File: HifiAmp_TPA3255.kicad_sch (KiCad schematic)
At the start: 125 parts, among them J1 PVDD 48V IN — NEEDS_DATA, J2 RCA L SE, J3 RCA R SE, J301 SPK_L, J302 SPK_R, J4 VOLUME_REMOTE, Q301 IPP330P10NM, Q302 IXTK200N10L2, U1 LM5010ASD, U2 LM2940IMP-12/NOPB, U3 TLV1117-33IDCY, U4 OPA1612AIDR, U5 OPA1612AIDR, U6 TPA3255B, U7 TPS3802K33DCKR, U8 LM5069-2

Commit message: feat(f1.7): add the WE-PD 1050 footprint, assign correct U1/L1 footprints in the schematic
Co-Authored-By: Claude Opus 5.5 <noreply@anthropic.com>
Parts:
- L1: footprint Inductor_SMD:L_Wuerth_WE-PD2-Typ-MS -> HifiAmp_TPA3255_Local:L_Wuerth_WE-PD-1050_10x10x5mm
- U1: footprint Package_SON:WSON-10-1EP_2.5x2.5mm_P0.5mm_EP1.2x2mm -> Package_SON:WSON-10-1EP_4x4mm_P0.8mm_EP2.6x3mm
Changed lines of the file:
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@@
 			)
 		)
-		(property "Footprint" "Package_SON:WSON-10-1EP_2.5x2.5mm_P0.5mm_EP1.2x2mm"
+		(property "Footprint" "Package_SON:WSON-10-1EP_4x4mm_P0.8mm_EP2.6x3mm"
 			(at 100.33 100.33 0)
 			(hide yes)
@@
 			)
 		)
-		(property "Footprint" "Inductor_SMD:L_Wuerth_WE-PD2-Typ-MS"
+		(property "Footprint" "HifiAmp_TPA3255_Local:L_Wuerth_WE-PD-1050_10x10x5mm"
 			(at 129.54 100.33 0)
 			(hide yes)

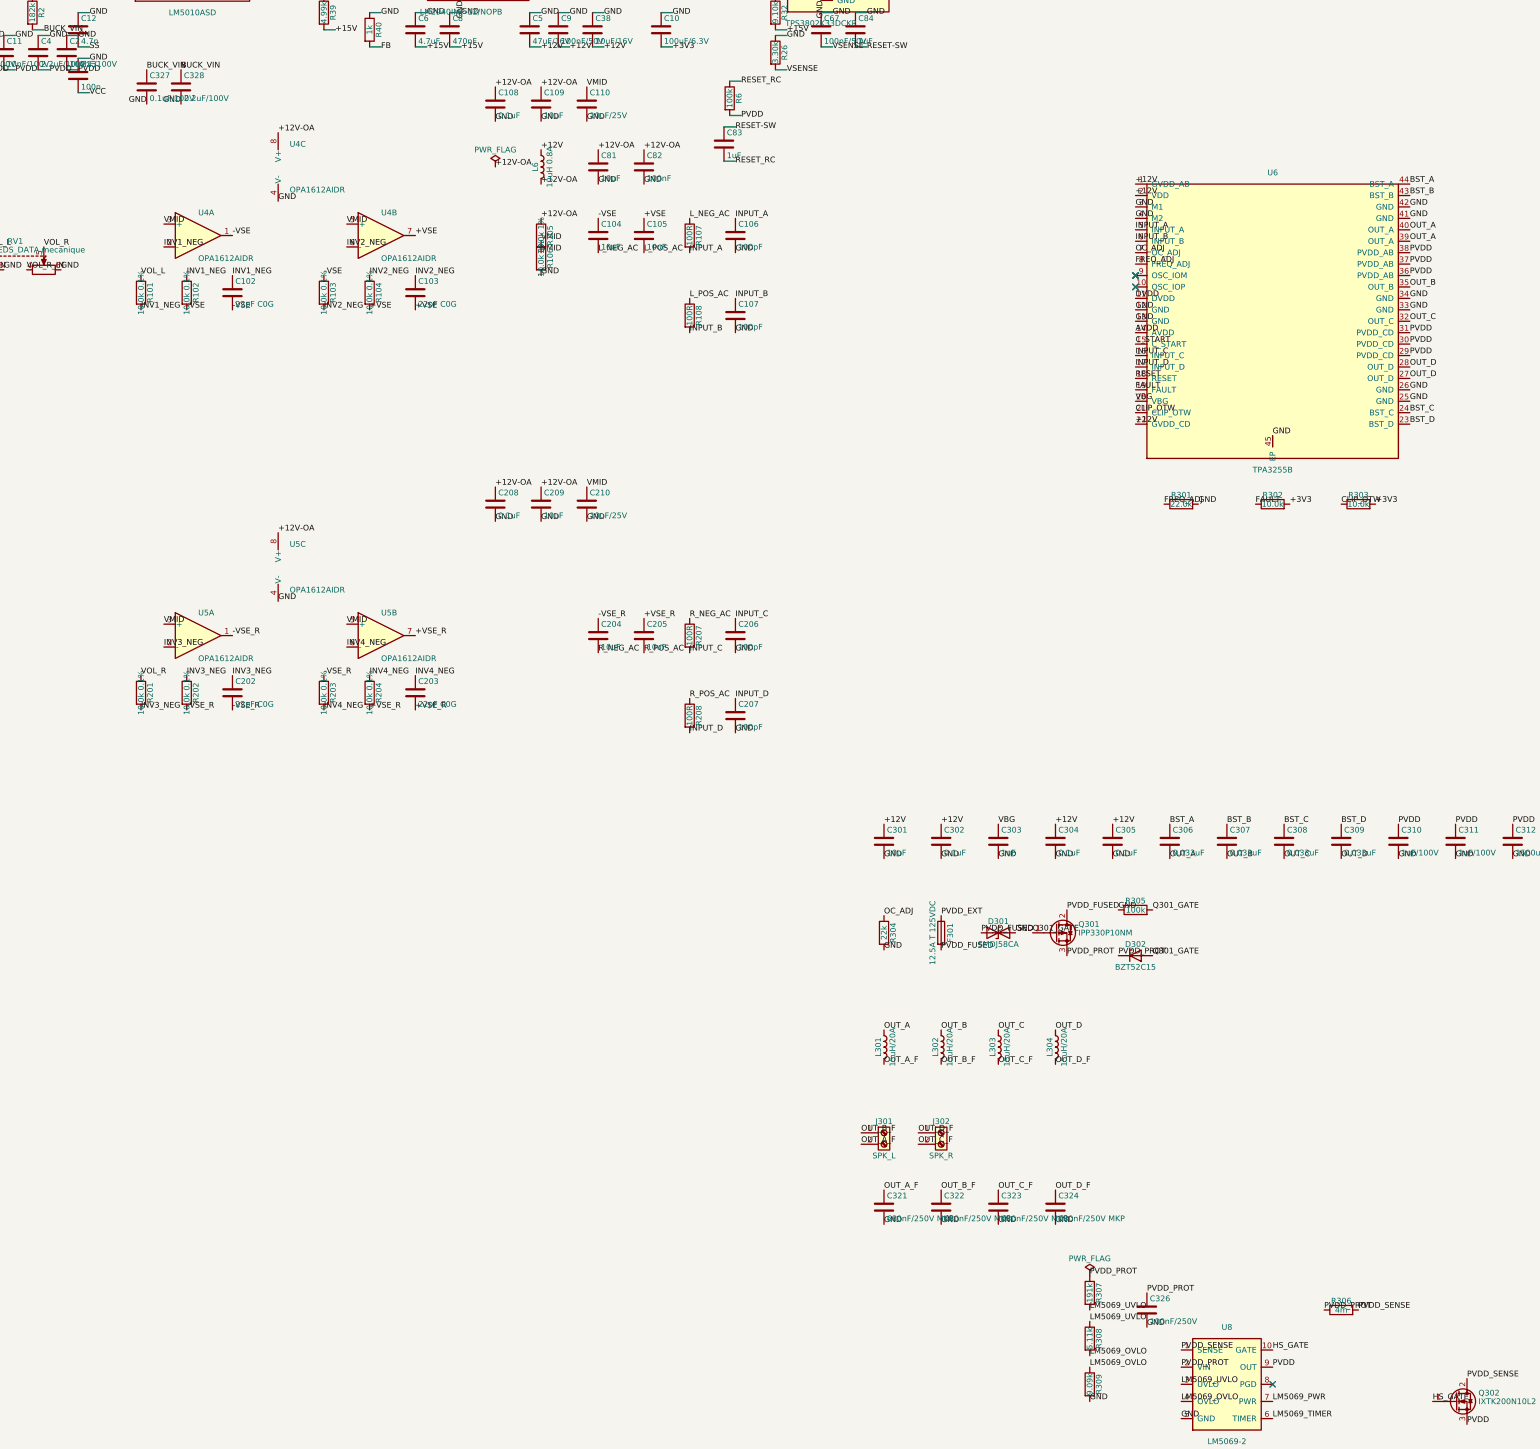
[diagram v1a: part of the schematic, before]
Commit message: feat(g1.3-b): set C13 to 1 µF, add C329 1 µF/100 V on PVDD_SENSE in the schematic
Co-Authored-By: Claude Opus 5.5 <noreply@anthropic.com>
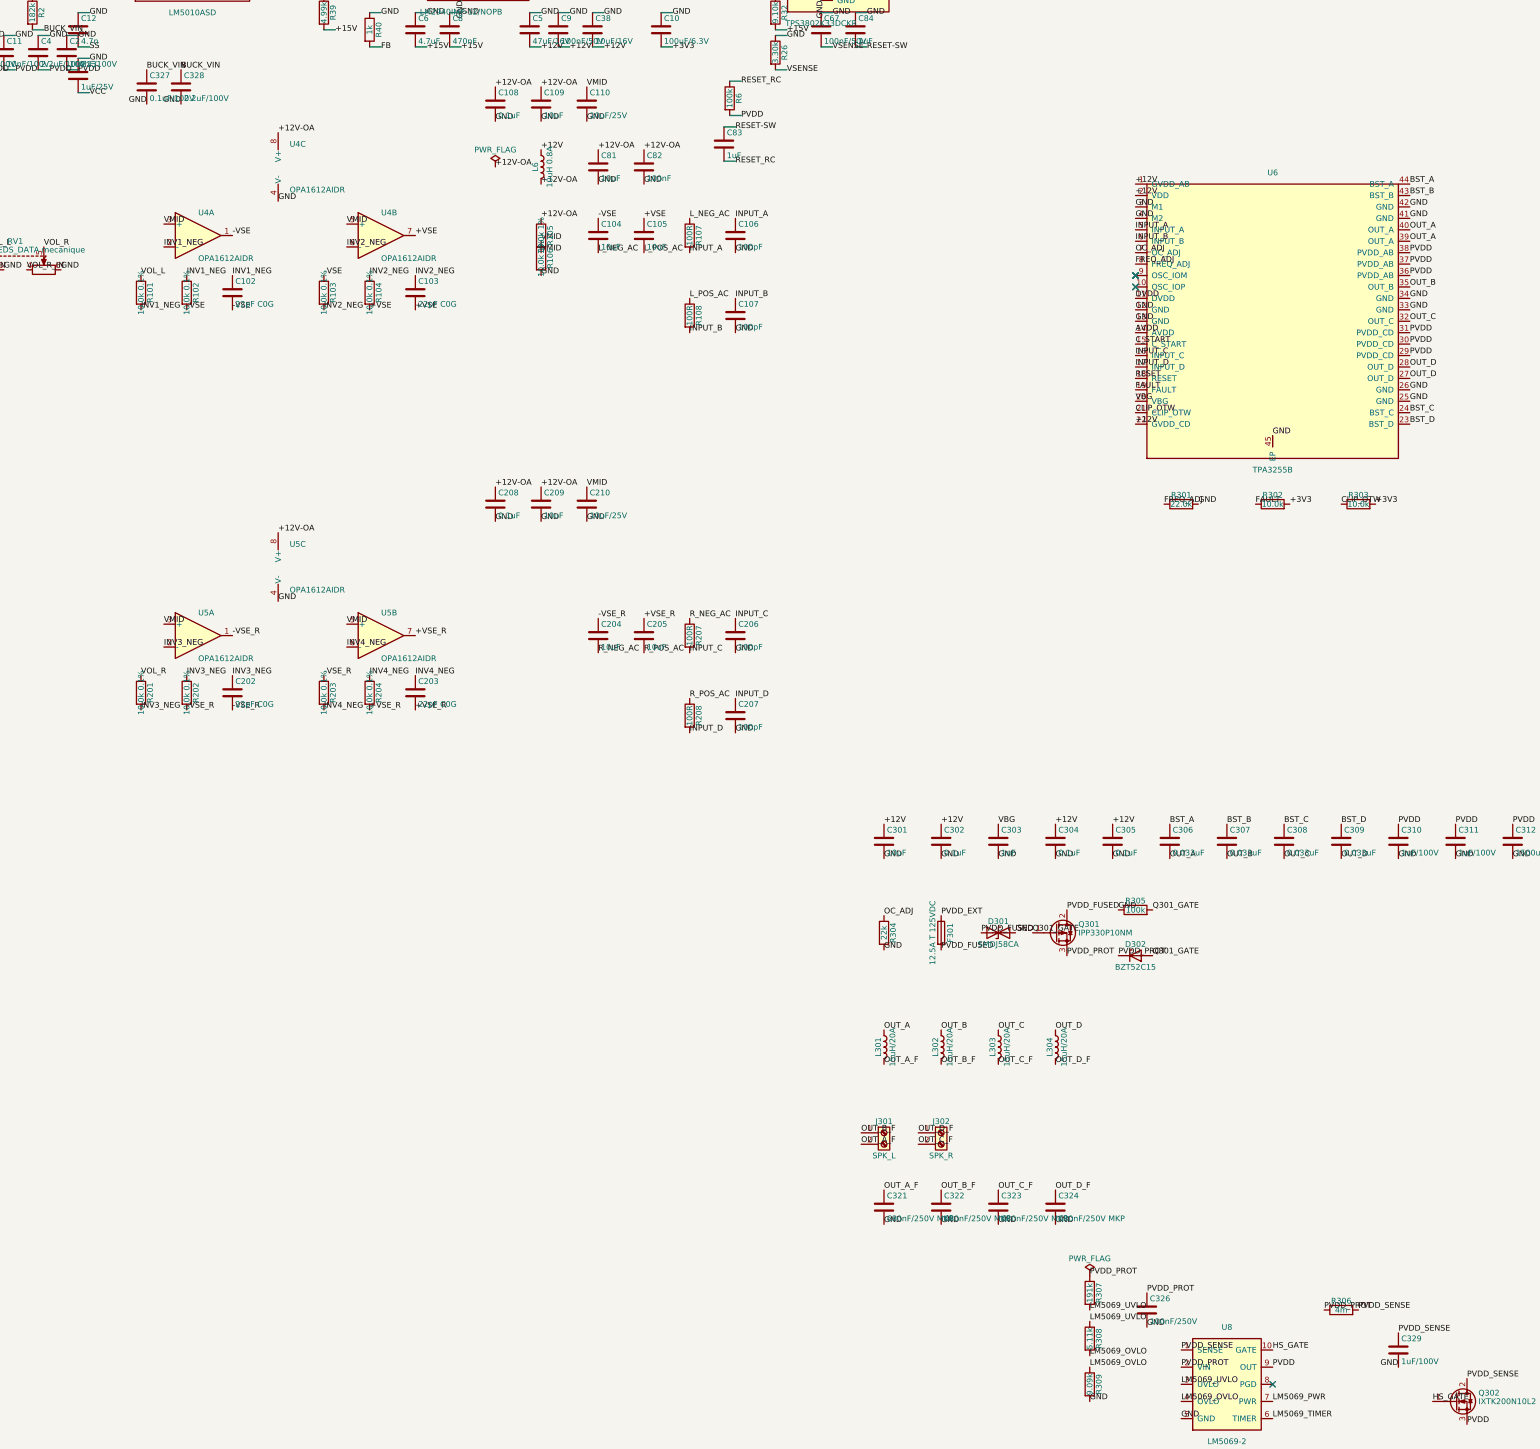
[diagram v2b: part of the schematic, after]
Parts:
- added C329: 1uF/100V, Capacitor_SMD:C_1210_3225Metric, symbol Device:C
- C13: value 100n -> 1uF/25V
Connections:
- net GND: now also C329.2
- net PVDD_SENSE: now also C329.1
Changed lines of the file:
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@@
 		)
 	)
+	(label "PVDD_SENSE"
+		(at 368.3 408.94 0)
+		(effects
+			(font
+				(size 1.27 1.27)
+			)
+			(justify left bottom)
+		)
+	)
+	(label "GND"
+		(at 368.3 416.56 180)
+		(effects
+			(font
+				(size 1.27 1.27)
+			)
+			(justify right bottom)
+		)
+	)
 	(symbol
 		(lib_id "HifiAmp_TPA3255_Local:LM5010ASD")
@@
 			)
 		)
-		(property "Value" "100n"
+		(property "Value" "1uF/25V"
 			(at 75.565 132.08 0)
 			(effects
@@
 					(unit 1)
 				)
+			)
+		)
+	)
+	(symbol
+		(lib_id "Device:C")
+		(at 368.3 412.75 0)
+		(unit 1)
+		(in_bom yes)
+		(on_board yes)
+		(dnp no)
+		(property "Reference" "C329"
+			(at 368.935 410.21 0)
+			(effects
+				(font
+					(size 1.27 1.27)
+				)
+				(justify left)
+			)
+		)
+		(property "Value" "1uF/100V"
+			(at 368.935 415.29 0)
+			(effects
+				(font
+					(size 1.27 1.27)
+				)
+				(justify left)
+			)
+		)
+		(property "Footprint" "Capacitor_SMD:C_1210_3225Metric"
+			(at 369.2652 416.56 0)
+			(hide yes)
+			(effects
+				(font
+					(size 1.27 1.27)
+				)
+			)
+		)
+		(property "Datasheet" ""
+			(at 368.3 412.75 0)
+			(hide yes)
+			(effects
+				(font
+					(size 1.27 1.27)
+				)
+			)
+		)
+		(instances
+			(project "HifiAmp_TPA3255"
+				(path "/82ac8e0a-ee6a-44b0-87ab-dda432df5a9b"
+					(reference "C329")
+					(unit 1)
+				)

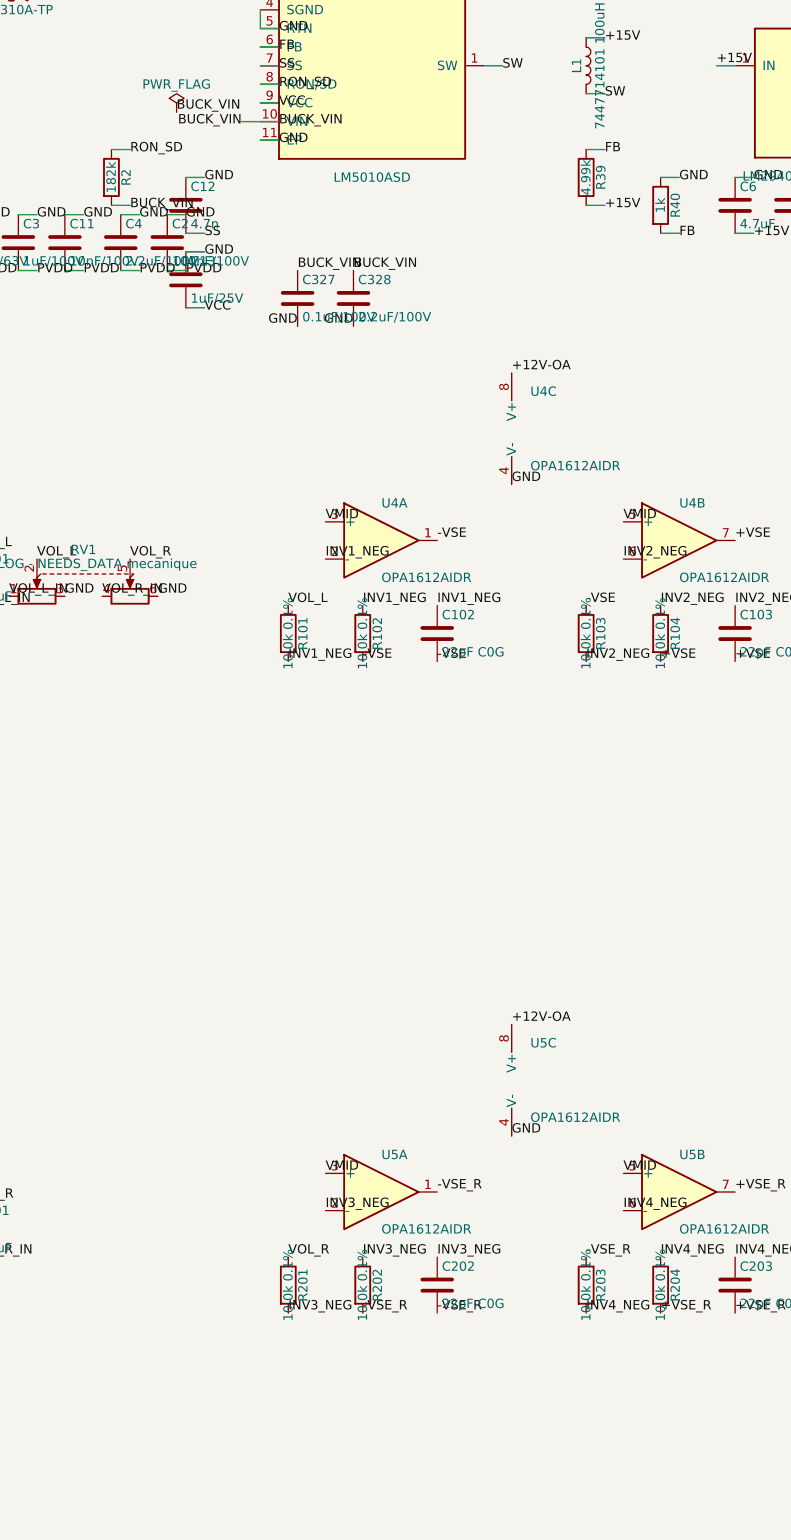
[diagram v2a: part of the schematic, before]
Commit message: feat(h1.4): add C111/C211 film series caps after the volume wiper and C7 on LM5010 FB
Co-Authored-By: Claude Opus 5.5 <noreply@anthropic.com>
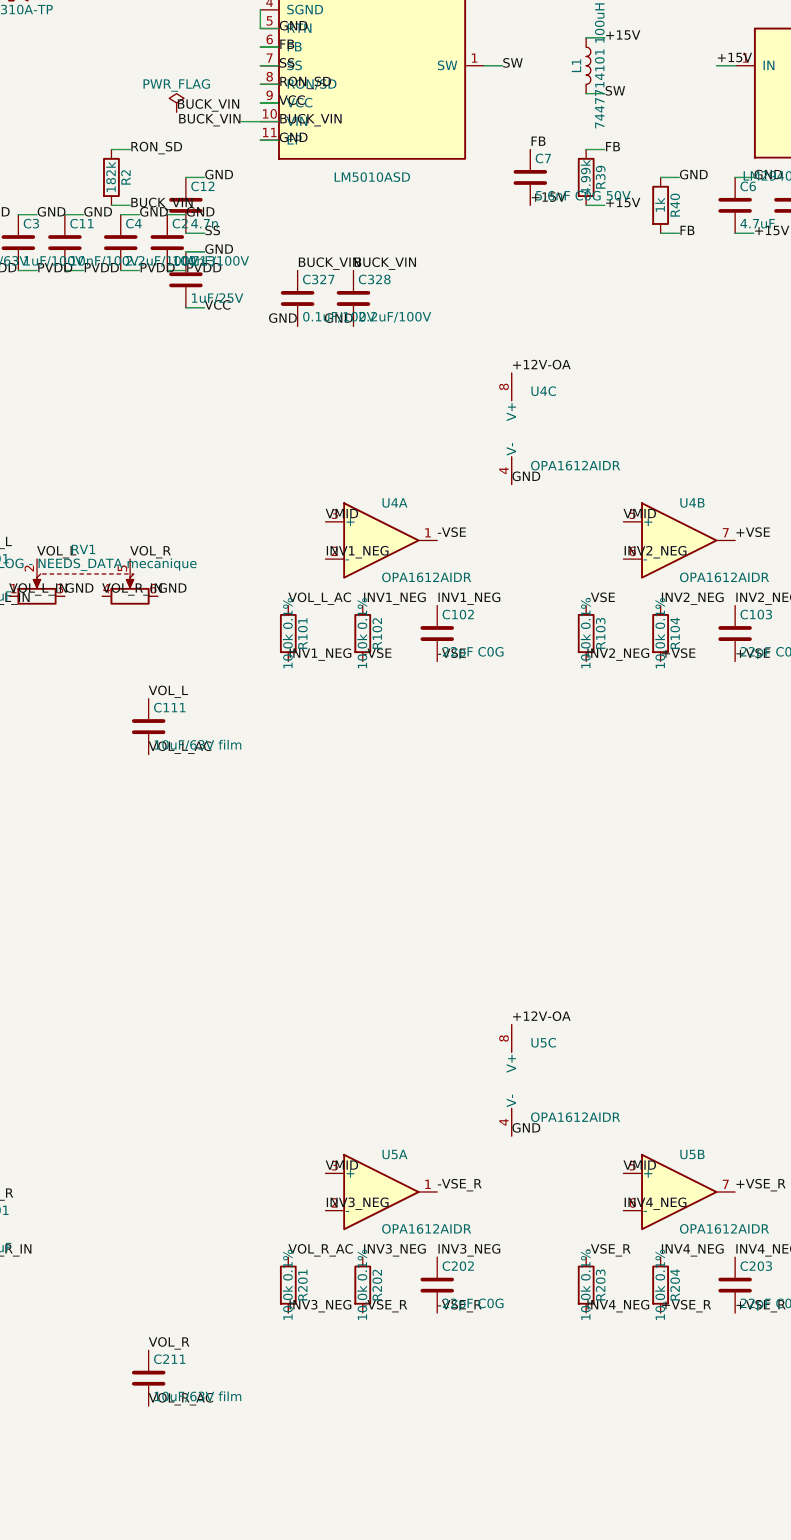
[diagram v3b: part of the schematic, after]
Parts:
- added C111, C211: 10uF/63V film, Capacitor_THT:C_Rect_L26.5mm_W10.5mm_P22.50mm_MKS4, symbol Device:C
- added C7: 5.6nF C0G 50V, Capacitor_SMD:C_0603_1608Metric, symbol Device:C
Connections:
- net +15V: now also C7.2
- net FB: now also C7.1
- net VOL_L: now also C111.1; no longer R101.1
- net VOL_R: now also C211.1; no longer R201.1
- new net VOL_L_AC: C111.2, R101.1
- new net VOL_R_AC: C211.2, R201.1
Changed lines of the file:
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@@
 		)
 	)
-	(label "VOL_L"
-		(at 88.9 173.99 0)
-		(effects
-			(font
-				(size 1.27 1.27)
-			)
-			(justify left bottom)
-		)
-	)
 	(label "INV1_NEG"
 		(at 88.9 181.61 0)
@@
 		)
 	)
-	(label "VOL_R"
-		(at 88.9 262.89 0)
-		(effects
-			(font
-				(size 1.27 1.27)
-			)
-			(justify left bottom)
-		)
-	)
 	(label "INV3_NEG"
 		(at 88.9 270.51 0)
@@
 		)
 	)
+	(label "VOL_L"
+		(at 69.85 186.69 0)
+		(effects
+			(font
+				(size 1.27 1.27)
+			)
+			(justify left bottom)
+		)
+	)
+	(label "VOL_L_AC"
+		(at 69.85 194.31 0)
+		(effects
+			(font
+				(size 1.27 1.27)
+			)
+			(justify left bottom)
+		)
+	)
+	(label "VOL_L_AC"
+		(at 88.9 173.99 0)
+		(effects
+			(font
+				(size 1.27 1.27)
+			)
+			(justify left bottom)
+		)
+	)
+	(label "VOL_R"
+		(at 69.85 275.59 0)
+		(effects
+			(font
+				(size 1.27 1.27)
+			)
+			(justify left bottom)
+		)
+	)
+	(label "VOL_R_AC"
+		(at 69.85 283.21 0)
+		(effects
+			(font
+				(size 1.27 1.27)
+			)
+			(justify left bottom)
+		)
+	)
+	(label "VOL_R_AC"
+		(at 88.9 262.89 0)
+		(effects
+			(font
+				(size 1.27 1.27)
+			)
+			(justify left bottom)
+		)
+	)
+	(label "FB"
+		(at 121.92 111.76 0)
+		(effects
+			(font
+				(size 1.27 1.27)
+			)
+			(justify left bottom)
+		)
+	)
+	(label "+15V"
+		(at 121.92 119.38 0)
+		(effects
+			(font
+				(size 1.27 1.27)
+			)
+			(justify left bottom)
+		)
+	)
 	(symbol
 		(lib_id "HifiAmp_TPA3255_Local:LM5010ASD")
@@
 					(unit 1)
 				)
+			)
+		)
+	)
+	(symbol
+		(lib_id "Device:C")
+		(at 69.85 190.5 0)
+		(unit 1)
+		(in_bom yes)
+		(on_board yes)
+		(dnp no)
+		(property "Reference" "C111"
+			(at 70.485 187.96 0)
+			(effects
+				(font
+					(size 1.27 1.27)
+				)
+				(justify left)
+			)
+		)
+		(property "Value" "10uF/63V film"
+			(at 70.485 193.04 0)
+			(effects
+				(font
+					(size 1.27 1.27)
+				)
+				(justify left)
+			)
+		)
+		(property "Footprint" "Capacitor_THT:C_Rect_L26.5mm_W10.5mm_P22.50mm_MKS4"
+			(at 70.8152 194.31 0)
+			(hide yes)
+			(effects
+				(font
+					(size 1.27 1.27)
+				)
+			)
+		)
+		(property "Datasheet" ""
+			(at 69.85 190.5 0)
+			(hide yes)
+			(effects
+				(font
+					(size 1.27 1.27)
+				)
+			)
+		)
+		(instances
+			(project "HifiAmp_TPA3255"
+				(path "/82ac8e0a-ee6a-44b0-87ab-dda432df5a9b"
+					(reference "C111")
+					(unit 1)
+				)
+			)
+		)
+	)
+	(symbol
+		(lib_id "Device:C")
+		(at 69.85 279.4 0)
+		(unit 1)
+		(in_bom yes)
+		(on_board yes)
+		(dnp no)
+		(property "Reference" "C211"
+			(at 70.485 276.86 0)
+			(effects
+				(font
+					(size 1.27 1.27)
+				)
+				(justify left)
+			)
+		)
+		(property "Value" "10uF/63V film"
+			(at 70.485 281.94 0)
+			(effects
+				(font
+					(size 1.27 1.27)
+				)
+				(justify left)
+			)
+		)
+		(property "Footprint" "Capacitor_THT:C_Rect_L26.5mm_W10.5mm_P22.50mm_MKS4"
+			(at 70.8152 283.21 0)
+			(hide yes)
+			(effects
+				(font
+					(size 1.27 1.27)
+				)
+			)
+		)
+		(property "Datasheet" ""
+			(at 69.85 279.4 0)
+			(hide yes)
+			(effects
+				(font
+					(size 1.27 1.27)
+				)
+			)
+		)
+		(instances
+			(project "HifiAmp_TPA3255"
+				(path "/82ac8e0a-ee6a-44b0-87ab-dda432df5a9b"
+					(reference "C211")
+					(unit 1)
+				)
+			)
+		)
+	)
+	(symbol
+		(lib_id "Device:C")
+		(at 121.92 115.57 0)
+		(unit 1)
+		(in_bom yes)
+		(on_board yes)
+		(dnp no)
+		(property "Reference" "C7"
+			(at 122.555 113.03 0)
+			(effects
+				(font
+					(size 1.27 1.27)
+				)
+				(justify left)
+			)
+		)
+		(property "Value" "5.6nF C0G 50V"
+			(at 122.555 118.11 0)
+			(effects
+				(font
+					(size 1.27 1.27)
+				)
+				(justify left)
+			)
+		)
+		(property "Footprint" "Capacitor_SMD:C_0603_1608Metric"
+			(at 122.8852 119.38 0)
+			(hide yes)
+			(effects
+				(font
+					(size 1.27 1.27)
+				)
+			)
+		)
+		(property "Datasheet" ""
+			(at 121.92 115.57 0)
+			(hide yes)
+			(effects
+				(font
+					(size 1.27 1.27)
+				)
+			)
+		)
+		(instances
+			(project "HifiAmp_TPA3255"
+				(path "/82ac8e0a-ee6a-44b0-87ab-dda432df5a9b"
+					(reference "C7")
+					(unit 1)
+				)
